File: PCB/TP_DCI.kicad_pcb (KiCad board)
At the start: 2 copper layers, 85.7 x 178.9 mm, 70 parts, among them J8 Molex_KK254, J9 Molex_KK254, K1 G5V-1, K2 G5V-1, P1 Conn_Poncho2P_2x_20x2, Q1 BC817W, Q2 BC817W, U1 PS2805-4, U2 ACS725xLCTR-10AU, U3 ACS725xLCTR-10AU, U4 DS3231, U5 24AA1025

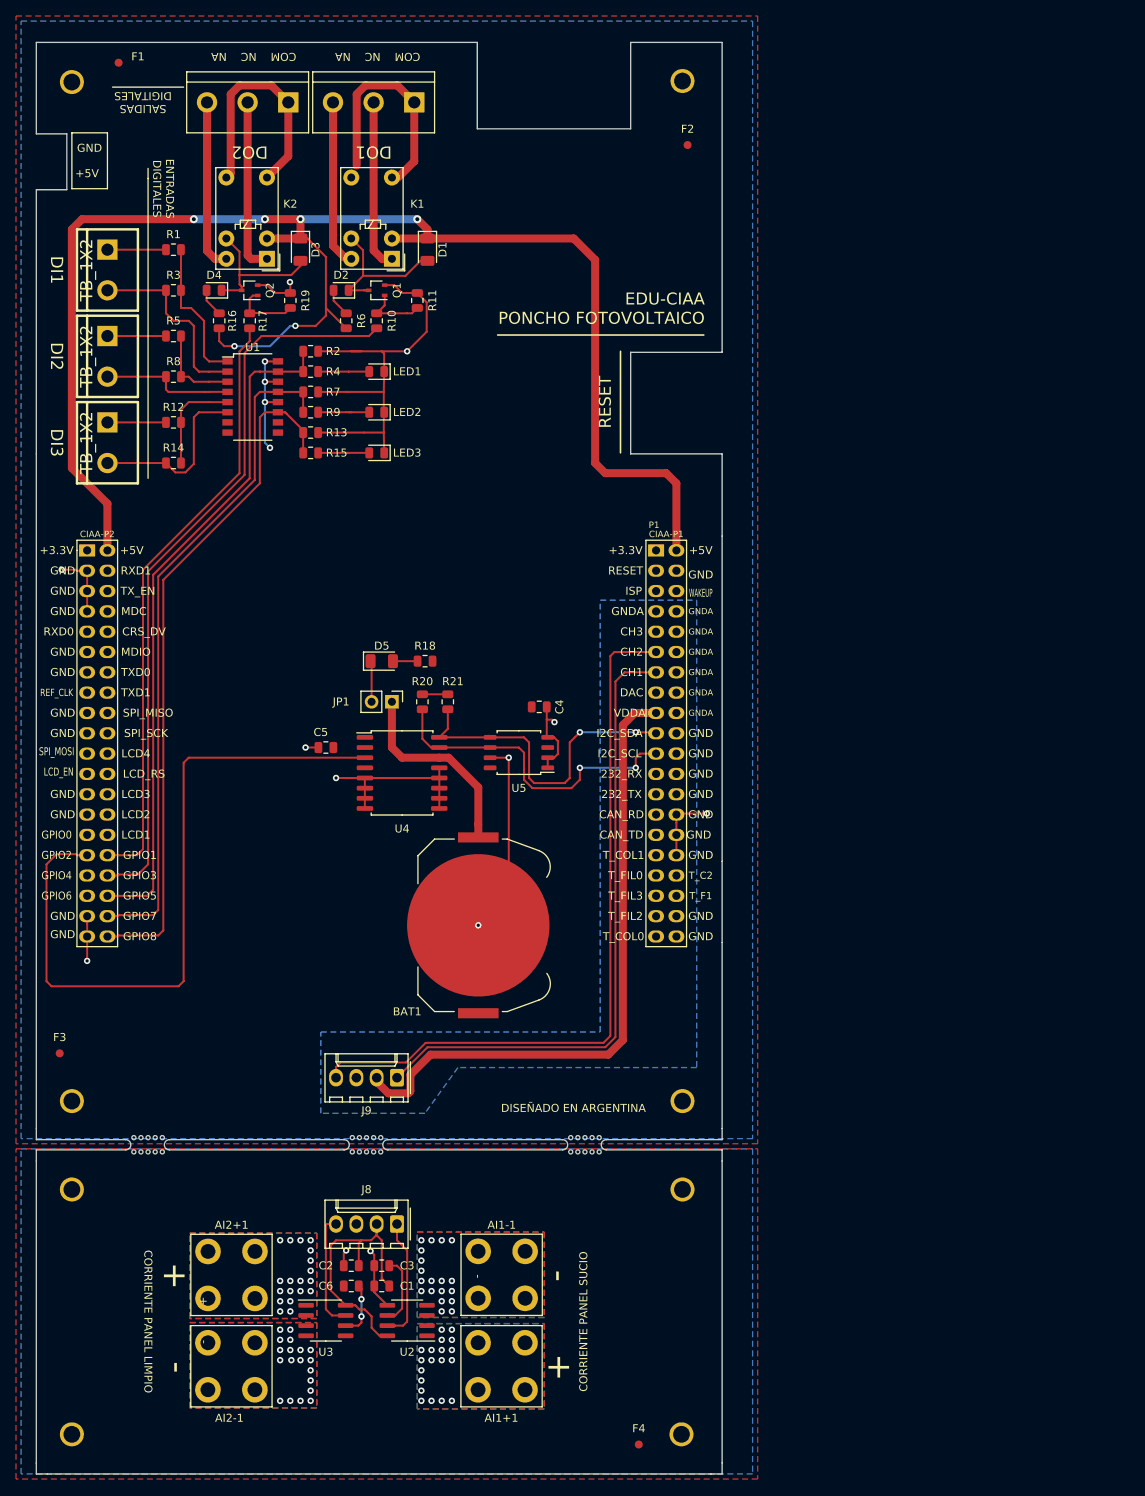
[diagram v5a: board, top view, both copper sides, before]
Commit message: Correcciones segun sugerencias del docente
- se incremento el ancho de tracks, tamaño de vias y clearance.
- el tamaño amplio del poncho se justifica por cuestiones mecánicas, para lograr mas puntos de anclaje a la EDU-CIAA
- se agregan comentarios para el fabricante.
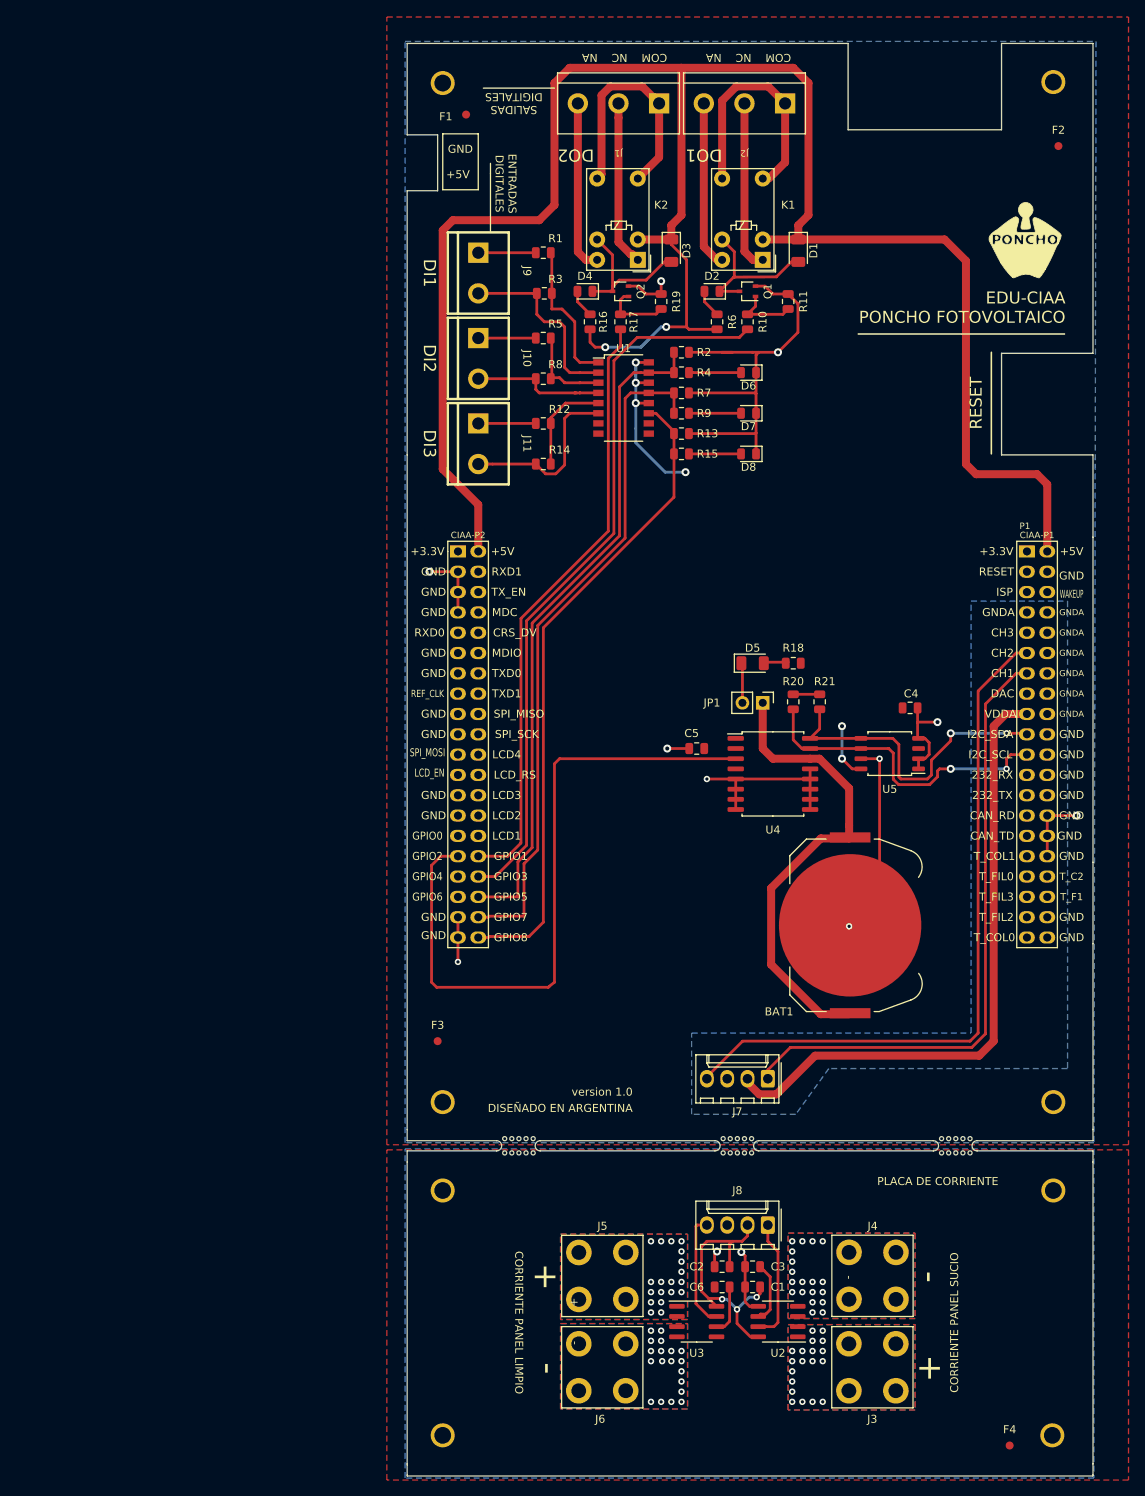
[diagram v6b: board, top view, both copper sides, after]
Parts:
- removed DI2: TB_1X2, Libreria_EDU_CIAA_NXP:bornier2
- removed DO1, DO2: TB_1X3, Libreria_EDU_CIAA_NXP:bornier3
- removed LED1, LED2, LED3: green, LED_SMD:LED_0805_2012Metric
- added D6: verde, LED_SMD:LED_0805_2012Metric, F.Cu at (108.7, 59.2)
- added D7: verde, LED_SMD:LED_0805_2012Metric, F.Cu at (108.7, 64.3)
- added D8: verde, LED_SMD:LED_0805_2012Metric, F.Cu at (108.7, 69.3)
- added G1: Logo_Poncho, Poncho_Esqueleto:Logo_Poncho, F.Cu at (143.3, 42.7)
- added J1: DO2, Libreria_EDU_CIAA_NXP:bornier3, F.Cu at (92.5, 25.5)
- added J10: DI2, Libreria_EDU_CIAA_NXP:bornier2, F.Cu at (74.9, 57.4)
- added J2: DO1, Libreria_EDU_CIAA_NXP:bornier3, F.Cu at (108.2, 25.5)
- J11: renamed from DI3; value TB_1X2 -> DI3
- J3: renamed from AI1+1; value TB_1X1 -> AI1(+)
- J4: renamed from AI1-1; value TB_1X1 -> AI1(-)
- J5: renamed from AI2+1; value TB_1X1 -> AI2(+)
- J6: renamed from AI2-1; value TB_1X1 -> AI2(-)
- J9: renamed from DI1; value TB_1X2 -> DI1
- moved F3 47.3 mm to (69.8, 142.7)
- moved BAT1 46.5 mm to (121.4, 128.3)
- moved R21 46.5 mm to (117.6, 100.3)
- moved J9 46.4 mm to (74.9, 46.7)
- moved R3 46.4 mm to (83.2, 49.3)
- moved D5 46.4 mm to (109.2, 95.5)
- moved H2 46.4 mm to (146.8, 161.4)
- moved H6 46.4 mm to (146.8, 22.9)
- moved H8 46.4 mm to (146.8, 150.4)
- moved C4 46.4 mm to (128.9, 101.1)
- moved D1 46.4 mm to (114.9, 43.9)
- moved D2 46.4 mm to (104.1, 49.0)
- moved D3 46.4 mm to (99.1, 43.9)
- moved D4 46.4 mm to (88.3, 49.0)
- moved F2 46.4 mm to (147.4, 30.9)
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- renumbered J9 to J7
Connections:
- net Net-(C1-Pad2) renamed GNDPWR
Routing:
- net +5V: track 198.6 -> 255.8 mm, vias 6 -> 2
- net Net-(BAT1-Pad1): track 24.8 -> 59.0 mm
- net +3V3: track 19.7 -> 34.4 mm, vias 4 -> 6
- net Net-(P1-Pad80): track 86.2 -> 80.9 mm
- net /GPIO2: track 88.2 -> 84.5 mm
- net /ADC_CH2: track 90.7 -> 87.2 mm
- net Net-(C1-Pad1): track 35.2 -> 32.0 mm, vias 0 -> 3
- net GND: track 142.9 -> 146.1 mm
- net /SDA: track 41.9 -> 39.6 mm
- net /COM1: track 27.7 -> 29.5 mm
- net Net-(P1-Pad74): track 92.4 -> 91.1 mm
- net /ADC_CH1: track 79.4 -> 78.2 mm
- net VDDA: track 80.2 -> 79.0 mm
- net /NC2: track 21.7 -> 20.7 mm
- net Net-(C3-Pad1): track 8.79 -> 7.75 mm
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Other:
- board size 85.7 x 178.9 mm -> 85.7 x 179.1 mm
- net class Default: clearance 0.3 -> 0.35; trace_width 0.25 -> 0.35
- rule pad_to_mask_clearance: 0.051 -> 0.1
- rule trace_clearance: 0.3 -> 0.35
- rule trace_min: 0.2 -> 0.35
- rule via_min_size: 0.4 -> 0.5
- board text added: "Material base: FR4 Espesor: 1.6mm Terminación: HASL Grillas: 10mils y 50mils Via: 1 mm / 0.5 mm Pistas: 0.35mm y 1 mm Margen: 0.35 mm"
- board text added: "PLACA DE CORRIENTE"
- board text added: "version 1.0"
